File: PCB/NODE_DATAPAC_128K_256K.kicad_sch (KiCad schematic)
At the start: 21 parts, among them J1 Conn_02x20_Odd_Even, U1 74161, U10/U14 62256-DIP, U2 74161, U3 74161, U4 74138, U5 74138, U6 74374, U7/U11 62256-DIP, U8/U12 62256-DIP, U9/U13 62256-DIP

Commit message: text notes
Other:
- note added: "ORIGINAL PARTS U1 U2 U3 SN74HC161N (TI) U4 U5 SN74HC138N (TI) U6 74HC374N (Phillips) U7 U8 U9 U10 P51256SL-10 (Intel) D1 1N4148 BAT1 PMB3.6B"
- note added: "There is only 13mm vertical space for the battery, and current replacement for PMB3.6B does not fit. 3/V65HT flat side-by-side fits in the space on the other side of the ribbon cable."
- moved on the sheet: TP2, TP3, TP4, U10/U14, U6, U8/U12, U9/U13

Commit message: VBUS to U5 /E3, notes, pcb layout no traces
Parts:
- BT1: footprint (none) -> 000_LOCAL:PMB3.6B
- D1: footprint Diode_THT:D_DO-41_SOD81_P10.16mm_Horizontal -> 000_LOCAL:D_DO-35_SOD27_P10.16mm_Horizontal
- J1: footprint (none) -> 000_LOCAL:IDC_to_board_2x20_flipped
- R1, R2, R3: footprint (none) -> 000_LOCAL:R_Axial_DIN0207_L6.3mm_D2.5mm_P10.16mm_Horizontal
- TP1, TP2, TP3, TP4: footprint (none) -> 000_LOCAL:TP_THT
- U1, U2, U3, U4, U5: footprint (none) -> 000_LOCAL:DIP-16_W7.62mm
- U10/U14, U7/U11, U8/U12, U9/U13: footprint Package_DIP:DIP-28_W15.24mm -> 000_LOCAL:DIP-28_W15.24mm
- U6: footprint (none) -> 000_LOCAL:DIP-20_W7.62mm
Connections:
- net RAM_RST: now also R3.2, U5.5 (E2); no longer D2.1 (K)
- net VBUS: now also R2.1, U5.6 (E3)
- net ~{BANK1_2}: now reaches TP3.1, U5.9 (O6)
- net ~{BANK0_3}: now reaches U10/U14.20 (~{CS}), U5.12 (O3)
- net ~{BANK0_0}: now reaches U5.15 (O0), U7/U11.20 (~{CS})
- net ~{BANK1_0}: now reaches TP1.1, U5.7 (O7)
- net ~{BANK1_3}: now reaches TP4.1, U5.11 (O4)
- net ~{BANK0_2}: now reaches U5.13 (O2), U9/U13.20 (~{CS})
- net ~{BANK1_1}: now reaches TP2.1, U5.10 (O5)
- net ~{BANK0_1}: now reaches U5.14 (O1), U8/U12.20 (~{CS})
- net +BATT: no longer names the net of BT1.1 (+), R1.2
- now unconnected: D2.2 (A)
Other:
- note added: "(piggybacked)"
- note added: "+5VDC"
- note added: "128K vs 256K Exterior case says 256K. Only 128K is actually installed. Circuit and PCB appears to support 256K by piggybacking another 4 SRAM on top of U7-U10. RAMDSK.CO displays "BANK #0", and has a "Bank" button that has no effect on a 128K unit. So the extra 128K would probably appear in the form of "BANK #1"."
- note added: "3.6V NiCD or NiMH"
- note added: "BANK #0"
- note added: "BANK #1"
- note added: "BUS CONNECTOR PIN NUMBERS Tandy used a non-standard pin numbering for the bus connector on models 102 & 200. The odd and even rows are flipped vs the standard numbering for those connectors. This drawing uses the Tandy numbering so that the schematic will match the 102 & 200 manuals, but this means you need to know not to use the standard numbering when dealing with the connector or cable. Exampl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"
- note added: "D2 RAM_RST BODGE Cut trace and insert diode. This appears to be specifically a user bodge, not a manufacturer bodge. * The strongest clue is the part 5082-2810 instead of just using another 1N4148. * One end of the diode is soldered directly to a thin trace instead of a pad, and not secured with glue either. * In 2 identical units, only one has this bodge."
- note added: "GND"
- note added: "NC"
- note added: "ORIGINAL PARTS (all same on 2 units) U1 U2 U3 SN74HC161N Texas Instruments U4 U5 SN74HC138N Texas Instruments U6 74HC374N Philips U7 U8 U9 U10 P51256SL-10 Intel D1 1N4148 BT1 PMB3.6B Plainview Batteries R1 200 R2 5.1k R3 240k"
- note added: "REPLACEMENT BATTERY There is only 13mm vertical space for the battery, and current replacement for PMB3.6B does not fit. FL3/V80H (3x V80H cells flat side-by-side) fits in a space on the other side of the ribbon cable. This only gives about 2.5 years with 128K installed and 1.25 years with 256K installed. Original capacity is unknown, but: * original cells are wider but also thinner, possibly lar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"
- note added: "USER BODGE ON ONE UNIT"
- note added: "VDD"
- note removed: "0.4VF"
- note removed: "2 identical units, both marked DATAPAC 256K on the outside. Both have only 128K installed. U5 pins 7,9,10,11 run to un-connected vias next to the same SRAM ~{CS} pins as U5 12,13,14,15. Probably 256K was made by piggybacking another set of 4 SRAM onto the existing set."
- note removed: "3-cell 3.6v NiCD or NiMH NO OTHERS"
- note removed: "D2 appears to be a user bodge, not original. In 2 identical units, only one has the bodge. All other components & values identical on both units."
- note removed: "ORIGINAL PARTS U1 U2 U3 SN74HC161N (TI) U4 U5 SN74HC138N (TI) U6 74HC374N (Phillips) U7 U8 U9 U10 P51256SL-10 (Intel) D1 1N4148 BAT1 PMB3.6B"
- note removed: "Optional 2nd 128K piggybacked DIPs. N/C but traces go as drawn."
- note removed: "There is only 13mm vertical space for the battery, and current replacement for PMB3.6B does not fit. 3/V65HT flat side-by-side fits in the space on the other side of the ribbon cable."
- moved on the sheet: BT1, D1, D2, R1, R2, R3, U4, U5

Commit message: WIP: PCB
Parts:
- added TP5: VMEM+, 000_LOCAL:TP_THT_pwr, symbol Connector:TestPoint
- added TP6: VMEM-, 000_LOCAL:TP_THT_pwr, symbol Connector:TestPoint
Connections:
- net GND: now also TP6.1
- net VBUS: now also J1.2 (Pin_2)
- net VMEM: now also TP5.1
- no-connect marks 39 -> 38
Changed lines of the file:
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@@
   (no_connect (at 53.34 109.22))
   (no_connect (at 139.7 219.71))
-  (no_connect (at 53.34 60.96))
   (no_connect (at 165.1 219.71))
   (no_connect (at 107.95 198.12))
@@
     )
   )
+  (symbol (lib_id "power:GND") (at 254 234.95 0) (unit 1)
+    (in_bom yes) (on_board yes) (dnp no)
+    (property "Reference" "#PWR041" (at 254 241.3 0)
+      (effects (font (size 1.27 1.27)) hide)
+    )
+    (property "Value" "GND" (at 254 238.76 0)
+      (effects (font (size 1.27 1.27)))
+    )
+    (property "Footprint" "" (at 254 234.95 0)
+      (effects (font (size 1.27 1.27)) hide)
+    )
+    (property "Datasheet" "" (at 254 234.95 0)
+      (effects (font (size 1.27 1.27)) hide)
+    )
+    (pin "1")
+    (instances
+      (project "NODE_DATAPAC_128K_256K"
+        (path "/f15c2929-5cf4-4b4e-965d-148e1bec8a42"
+          (reference "#PWR041") (unit 1)
+        )
+      )
+    )
+  )
   (symbol (lib_id "power:GND") (at 53.34 104.14 90) (unit 1)
     (in_bom yes) (on_board yes) (dnp no) (fields_autoplaced)
@@
     )
   )
+  (symbol (lib_id "power:VBUS") (at 53.34 60.96 270) (unit 1)
+    (in_bom yes) (on_board yes) (dnp no)
+    (property "Reference" "#PWR042" (at 49.53 60.96 0)
+      (effects (font (size 1.27 1.27)) hide)
+    )
+    (property "Value" "VBUS" (at 58.42 60.96 90)
+      (effects (font (size 1.27 1.27)))
+    )
+    (property "Footprint" "" (at 53.34 60.96 0)
+      (effects (font (size 1.27 1.27)) hide)
+    )
+    (property "Datasheet" "" (at 53.34 60.96 0)
+      (effects (font (size 1.27 1.27)) hide)
+    )
+    (pin "1")
+    (instances
+      (project "NODE_DATAPAC_128K_256K"
+        (path "/f15c2929-5cf4-4b4e-965d-148e1bec8a42"
+          (reference "#PWR042") (unit 1)
+        )
+      )
+    )
+  )
   (symbol (lib_id "power:VMEM") (at 152.4 123.19 0) (unit 1)
     (in_bom yes) (on_board yes) (dnp no)
@@
     )
   )
+  (symbol (lib_id "power:VMEM") (at 245.11 234.95 180) (unit 1)
+    (in_bom yes) (on_board yes) (dnp no)
+    (property "Reference" "#PWR021" (at 245.11 231.14 0)
+      (effects (font (size 1.27 1.27)) hide)
+    )
+    (property "Value" "VMEM" (at 245.11 238.76 0)
+      (effects (font (size 1.27 1.27)))
+    )
+    (property "Footprint" "" (at 245.11 234.95 0)
+      (effects (font (size 1.27 1.27)) hide)
+    )
+    (property "Datasheet" "" (at 245.11 234.95 0)
+      (effects (font (size 1.27 1.27)) hide)
+    )
+    (pin "1")
+    (instances
+      (project "NODE_DATAPAC_128K_256K"
+        (path "/f15c2929-5cf4-4b4e-965d-148e1bec8a42"
+          (reference "#PWR021") (unit 1)
+        )
+      )
+    )
+  )
   (symbol (lib_id "power:VBUS") (at 139.7 224.79 90) (unit 1)
     (in_bom yes) (on_board yes) (dnp no)
@@
     )
   )
+  (symbol (lib_id "Connector:TestPoint") (at 254 234.95 0) (unit 1)
+    (in_bom yes) (on_board yes) (dnp no)
+    (property "Reference" "TP6" (at 254 229.87 0)
+      (effects (font (size 1.27 1.27)))
+    )
+    (property "Value" "VMEM-" (at 254 228.6 0)
+      (effects (font (size 1.27 1.27)) (justify bottom))
+    )
+    (property "Footprint" "000_LOCAL:TP_THT_pwr" (at 259.08 234.95 0)
+      (effects (font (size 1.27 1.27)) hide)
+    )
+    (property "Datasheet" "~" (at 259.08 234.95 0)
+      (effects (font (size 1.27 1.27)) hide)
+    )
+    (pin "1")
+    (instances
+      (project "NODE_DATAPAC_128K_256K"
+        (path "/f15c2929-5cf4-4b4e-965d-148e1bec8a42"
+          (reference "TP6") (unit 1)
+        )
+      )
+    )
+  )
   (symbol (lib_id "Connector:TestPoint") (at 389.89 85.09 0) (unit 1)
     (in_bom yes) (on_board yes) (dnp no)
@@
         )
       )
+    )
+  )
+  (symbol (lib_id "Connector:TestPoint") (at 245.11 234.95 0) (unit 1)
+    (in_bom yes) (on_board yes) (dnp no)
+    (property "Reference" "TP5" (at 245.11 229.87 0)
+      (effects (font (size 1.27 1.27)))
+    )
+    (property "Value" "VMEM+" (at 245.11 228.6 0)
+      (effects (font (size 1.27 1.27)) (justify bottom))
+    )
+    (property "Footprint" "000_LOCAL:TP_THT_pwr" (at 250.19 234.95 0)
+      (effects (font (size 1.27 1.27)) hide)
+    )
+    (property "Datasheet" "~" (at 250.19 234.95 0)
+      (effects (font (size 1.27 1.27)) hide)
+    )
+    (pin "1")
+    (instances
+      (project "NODE_DATAPAC_128K_256K"
+        (path "/f15c2929-5cf4-4b4e-965d-148e1bec8a42"
+          (reference "TP5") (unit 1)
+        )
+      )

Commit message: PCB!
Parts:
- U10/U14, U7/U11, U8/U12, U9/U13: value 62256-DIP -> 62256
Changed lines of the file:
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@@
     (title "NODE DATAPAC 128K-256K")
     (date "2023-08-19")
-    (rev "002")
+    (rev "003")
     (company "Brian K. White - b.kenyon.w@gmail.com")
     (comment 1 "Schematic re-created from manual examination of physical units, not yet proven.")
@@
       (effects (font (size 1.27 1.27)) (justify left))
     )
-    (property "Value" "62256-DIP" (at 374.3041 53.34 0)
+    (property "Value" "62256" (at 374.3041 53.34 0)
       (effects (font (size 1.27 1.27)) (justify left))
     )
@@
       (effects (font (size 1.27 1.27)) (justify left))
     )
-    (property "Value" "62256-DIP" (at 218.0941 53.34 0)
+    (property "Value" "62256" (at 218.0941 53.34 0)
       (effects (font (size 1.27 1.27)) (justify left))
     )
@@
       (effects (font (size 1.27 1.27)) (justify left))
     )
-    (property "Value" "62256-DIP" (at 320.9641 53.34 0)
+    (property "Value" "62256" (at 320.9641 53.34 0)
       (effects (font (size 1.27 1.27)) (justify left))
     )
@@
       (effects (font (size 1.27 1.27)) (justify left))
     )
-    (property "Value" "62256-DIP" (at 271.4341 53.34 0)
+    (property "Value" "62256" (at 271.4341 53.34 0)
       (effects (font (size 1.27 1.27)) (justify left))
     )

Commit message: sch notes
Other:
- note added: "74161 NC INPUTS Yes really no connection to GND or VCC or anything else! SN74HC161N datasheet does give the standard rule: "All unused inputs of the device must be held at VCC or GND""
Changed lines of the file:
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@@
+    (effects (font (size 1.27 1.27)) (justify left bottom))
+  )
+  (text "74161 NC INPUTS\nYes really no connection to GND\nor VCC or anything else!\nSN74HC161N datasheet does\ngive the standard rule:\n\"All unused inputs of the device\nmust be held at VCC or GND\""
+    (at 17.78 241.3 0)
     (effects (font (size 1.27 1.27)) (justify left bottom))
   )

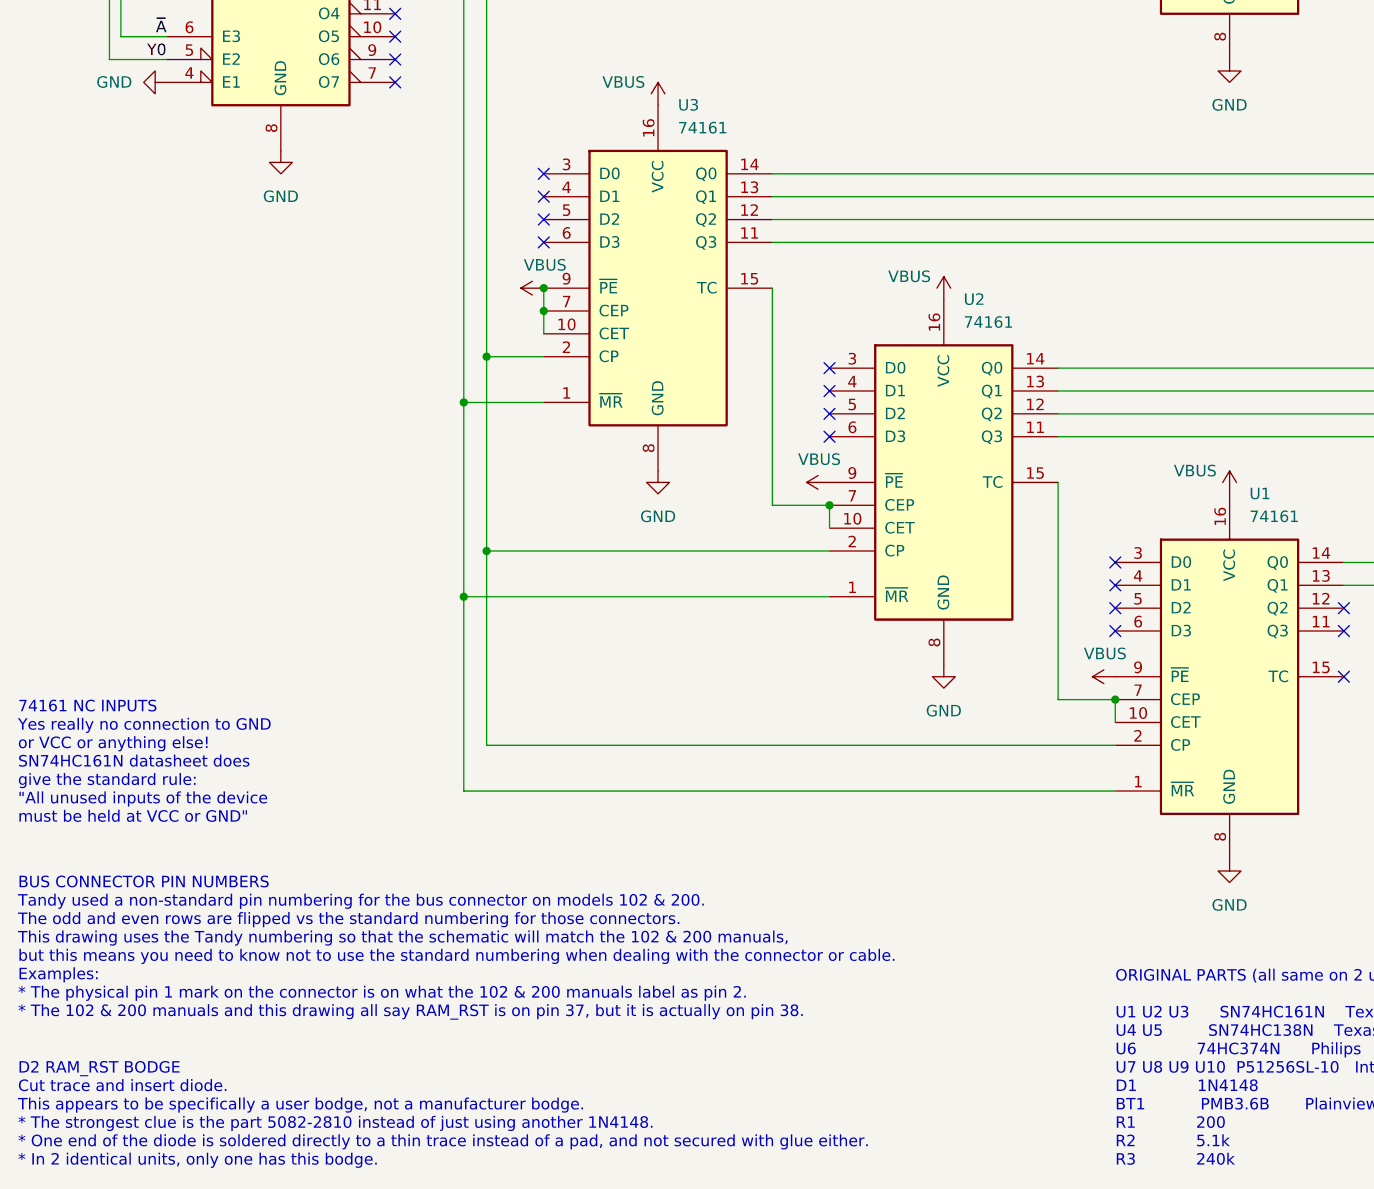
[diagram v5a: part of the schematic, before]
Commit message: optimize some traces
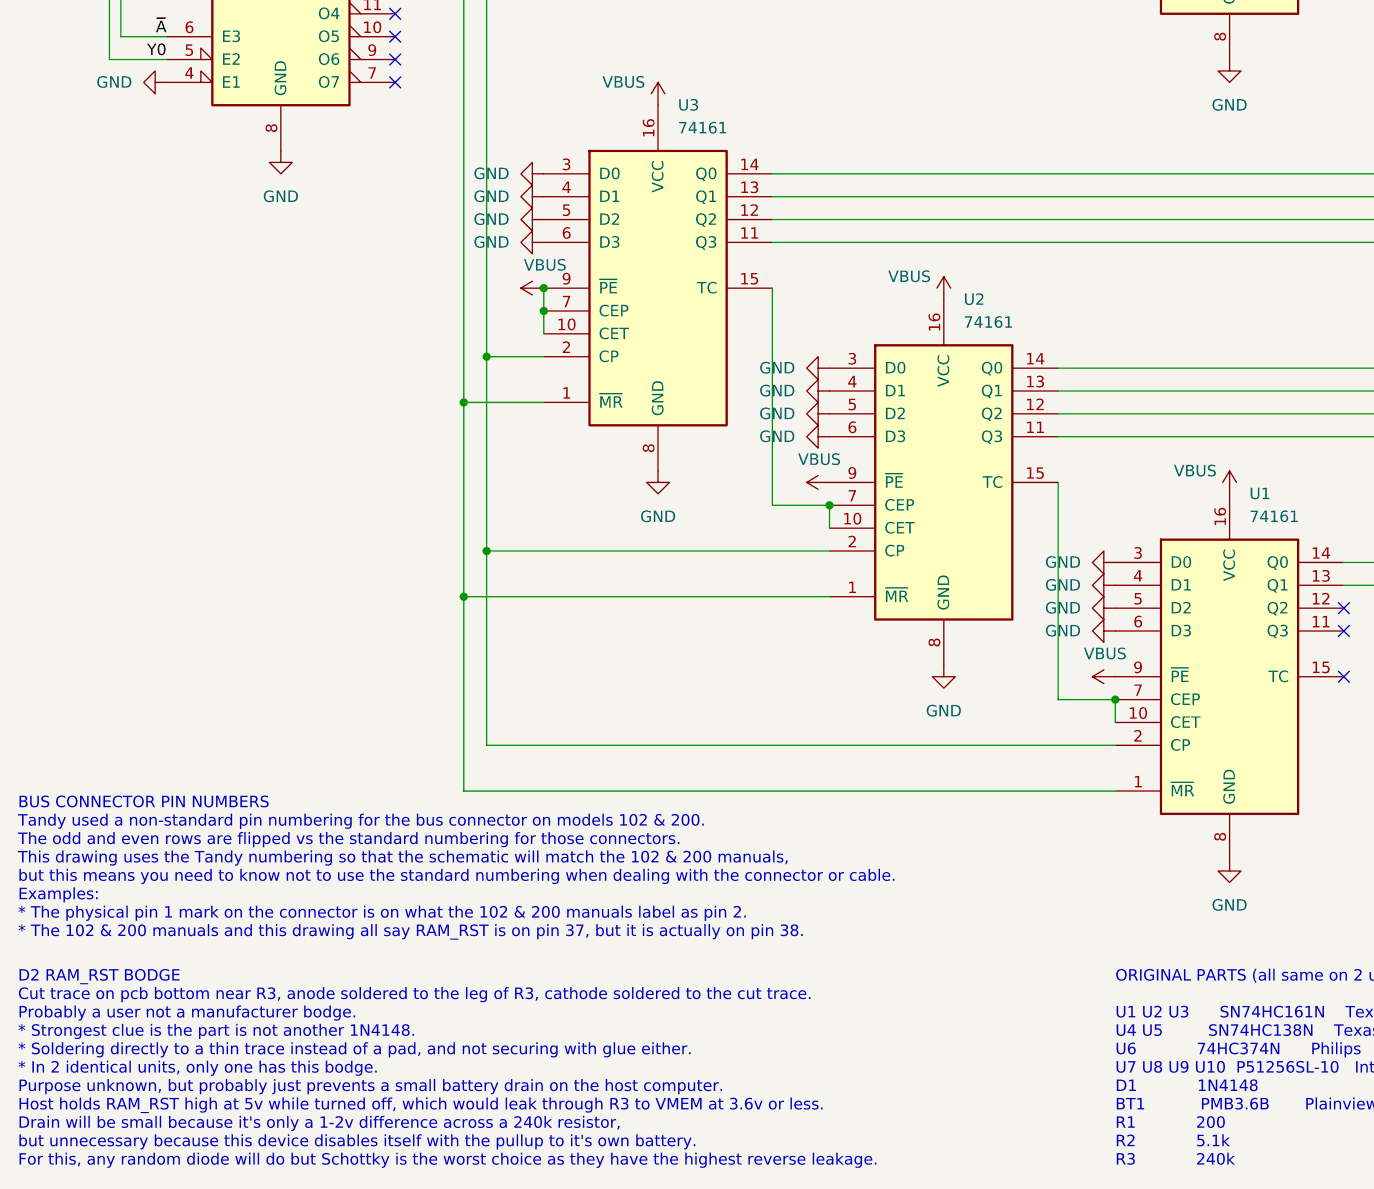
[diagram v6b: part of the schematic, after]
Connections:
- net GND: now also U1.3 (D0), U1.4 (D1), U1.5 (D2), U1.6 (D3), U2.3 (D0), U2.4 (D1), U2.5 (D2), U2.6 (D3), U3.3 (D0), U3.4 (D1), U3.5 (D2), U3.6 (D3)
- no-connect marks 38 -> 26
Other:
- note added: "D2 RAM_RST BODGE Cut trace on pcb bottom near R3, anode soldered to the leg of R3, cathode soldered to the cut trace. Probably a user not a manufacturer bodge. * Strongest clue is the part is not another 1N4148. * Soldering directly to a thin trace instead of a pad, and not securing with glue either. * In 2 identical units, only one has this bodge. Purpose unknown, but probably just prevents a sm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"
- note removed: "74161 NC INPUTS Yes really no connection to GND or VCC or anything else! SN74HC161N datasheet does give the standard rule: "All unused inputs of the device must be held at VCC or GND""
- note removed: "D2 RAM_RST BODGE Cut trace and insert diode. This appears to be specifically a user bodge, not a manufacturer bodge. * The strongest clue is the part 5082-2810 instead of just using another 1N4148. * One end of the diode is soldered directly to a thin trace instead of a pad, and not secured with glue either. * In 2 identical units, only one has this bodge."
